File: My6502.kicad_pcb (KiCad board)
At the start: 2 copper layers, 99.7 x 99.7 mm, 28 parts, among them J1 IRQ_SEL, J2 CLK Jumper, J4 Expansion Port, J5 IRQ_Pullup, SW1 RESET, U1 ROM 28C256, U2 CPU 6502, U3 RAM 62256, U4 74HCT00, U5 74HCT02, U6 DS1813-10, U7 74LS21, X1 CXO_DIP14

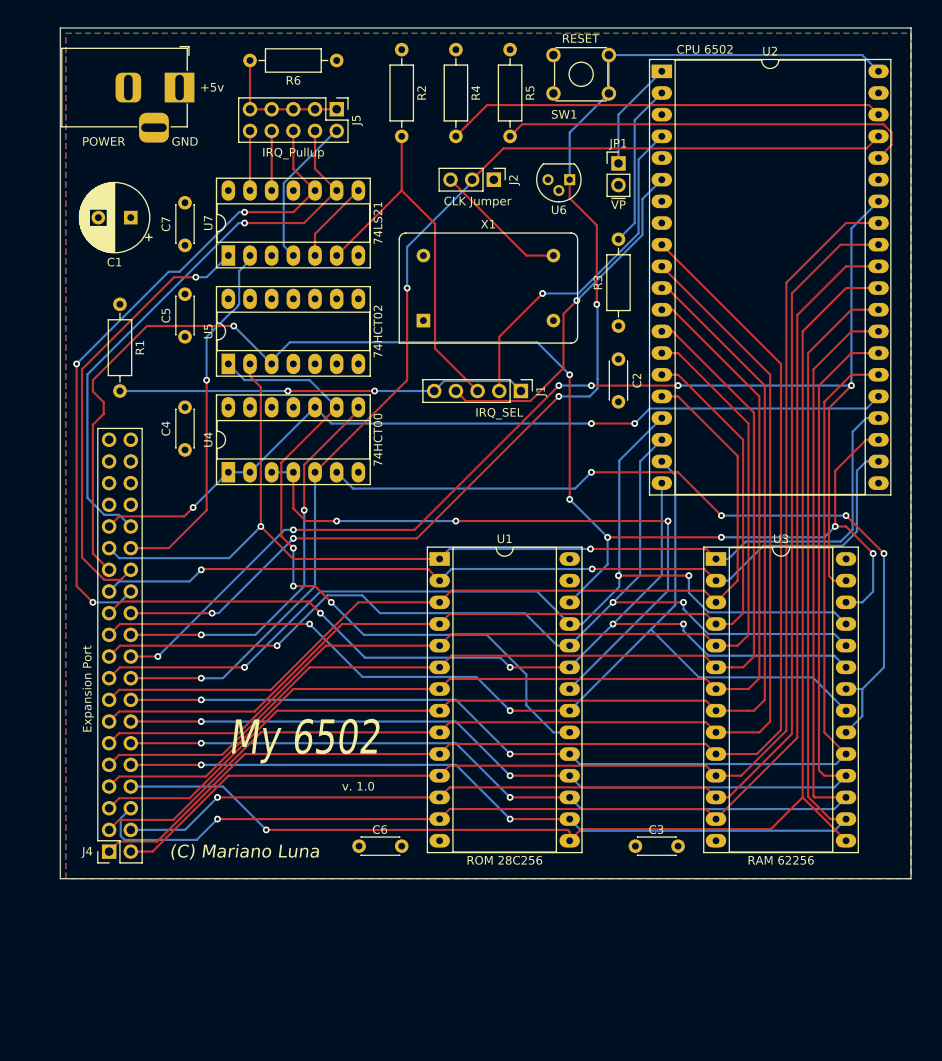
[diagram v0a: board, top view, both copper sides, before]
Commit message: Components Placed - missing wiring the VIA
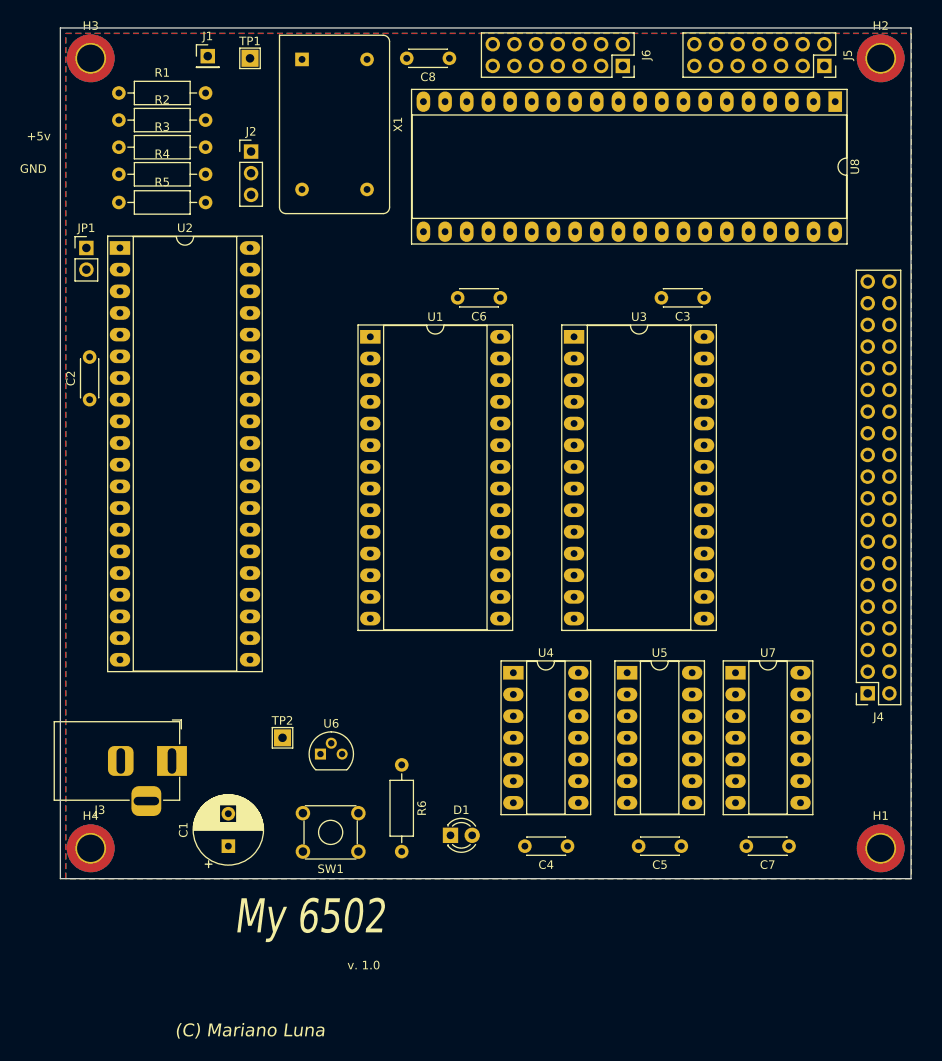
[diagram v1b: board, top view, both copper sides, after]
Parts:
- removed POWER: Barrel_Jack_Switch, Connector_BarrelJack:BarrelJack_Horizontal
- added C8: 0.1uF, Capacitor_THT:C_Disc_D4.3mm_W1.9mm_P5.00mm, F.Cu at (76.7, 53.7)
- added D1: LED, LED_THT:LED_D3.0mm, F.Cu at (76.8, 144.8)
- added H1: MNT, MountingHole:MountingHole_3.2mm_M3_DIN965_Pad_TopBottom, F.Cu at (127.3, 146.3)
- added H2: MNT, MountingHole:MountingHole_3.2mm_M3_DIN965_Pad_TopBottom, F.Cu at (127.3, 53.7)
- added H3: MNT, MountingHole:MountingHole_3.2mm_M3_DIN965_Pad_TopBottom, F.Cu at (34.7, 53.7)
- added H4: MNT, MountingHole:MountingHole_3.2mm_M3_DIN965_Pad_TopBottom, F.Cu at (34.7, 146.3)
- added J3: Power 5V, Connector_BarrelJack:BarrelJack_Horizontal, F.Cu at (44.2, 136.1)
- added J6: Port B, Connector_PinSocket_2.54mm:PinSocket_2x07_P2.54mm_Vertical, F.Cu at (97.0, 54.6)
- added TP1: CLK, TestPoint:TestPoint_THTPad_2.0x2.0mm_Drill1.0mm, F.Cu at (53.3, 53.7)
- added TP2: ~RESET, TestPoint:TestPoint_THTPad_2.0x2.0mm_Drill1.0mm, F.Cu at (57.1, 133.3)
- added U8: WD65C22, Package_DIP:DIP-40_W15.24mm_Socket_LongPads, F.Cu at (121.9, 58.8)
- C1: value 1000uF -> 100uF
- J1: value IRQ_SEL -> ~NMI; footprint Connector_PinHeader_2.54mm:PinHeader_1x05_P2.54mm_Vertical -> Connector_PinHeader_2.54mm:PinHeader_1x01_P2.54mm_Vertical
- J4: value Expansion Port -> Expansion Bus
- J5: value IRQ_Pullup -> Port A; footprint Connector_PinHeader_2.54mm:PinHeader_2x05_P2.54mm_Vertical -> Connector_PinSocket_2.54mm:PinSocket_2x07_P2.54mm_Vertical
- R1, R2, R3, R4, R5: value 4K7 -> 3K3
- R6: value 4K7 -> 150
- U2: value CPU 6502 -> WD65C02; footprint Package_DIP:DIP-40_W25.4mm_Socket_LongPads -> Package_DIP:DIP-40_W15.24mm_Socket_LongPads
- X1: value CXO_DIP14 -> OSC
- moved C7 99.8 mm to (116.5, 146.1), turned to 180 degrees
- moved SW1 96.1 mm to (66.0, 146.7), turned to 180 degrees
- moved J4 90.8 mm to (125.7, 128.1)
- moved C5 83.3 mm to (103.9, 146.1), turned to 180 degrees
- moved R6 82.9 mm to (71.1, 136.5), turned to 270 degrees
- moved U7 77.0 mm to (110.2, 125.7), turned to 0 degrees
- moved C1 74.5 mm to (50.8, 146.1), turned to 90 degrees
- moved U6 73.4 mm to (61.6, 135.3), turned to 0 degrees
- moved U2 66.8 mm to (38.1, 75.9)
- moved C6 66.4 mm to (82.7, 81.8), turned to 180 degrees
- moved C3 64.8 mm to (106.6, 81.8), turned to 180 degrees
- moved C4 64.5 mm to (90.6, 146.1), turned to 180 degrees
- moved JP1 63.1 mm to (34.2, 75.9)
- moved R3 62.2 mm to (38.0, 64.1), turned to 0 degrees
- moved C2 62.2 mm to (34.5, 93.7), turned to 90 degrees
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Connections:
- net /CLK_OUT renamed Net-(J2-Pad3)
- J1 pad 1: Net-(J1-Pad1) -> ~NMI
- J4 pad 1: a0 -> GND
- J4 pad 10: d4 -> d3
- J4 pad 11: a5 -> a4
- J4 pad 12: d5 -> d4
- J4 pad 13: a6 -> a5
- J4 pad 14: d6 -> d5
- J4 pad 15: a7 -> a6
- J4 pad 16: d7 -> d6
- J4 pad 17: a8 -> a7
- J4 pad 18: CLK -> d7
- J4 pad 19: a9 -> a8
- J4 pad 2: d0 -> +5V
- J4 pad 20: R~W -> PHI2
- J4 pad 21: a10 -> a9
- J4 pad 22: ~IO_CS -> R~W
- J4 pad 23: a11 -> a10
- J4 pad 24: ~RESET -> ~IO_CS
- J4 pad 25: a12 -> a11
- J4 pad 26: EXP_IRQ -> ~RESET
- J4 pad 27: a13 -> a12
- J4 pad 28: ~VIA1_IRQ -> ~VIA2_IRQ
- J4 pad 29: a14 -> a13
- J4 pad 3: a1 -> a0
- J4 pad 30: ~VIA2_IRQ -> EXP_IRQ
- J4 pad 31: a15 -> a14
- J4 pad 33: Net-(J4-Pad33) -> a15
- J4 pad 34: Net-(J4-Pad34) -> ~NMI
- J4 pad 38: GND -> Net-(J4-Pad38)
- J4 pad 39: Net-(J4-Pad39) -> +5V
- J4 pad 4: d1 -> d0
- J4 pad 40: +5V -> GND
- J4 pad 5: a2 -> a1
- J4 pad 6: d2 -> d1
- J4 pad 7: a3 -> a2
- J4 pad 8: d3 -> d2
- J4 pad 9: a4 -> a3
- J5 pad 1: Net-(J5-Pad1) -> GND
- J5 pad 10: Net-(J5-Pad10) -> PA7
- J5 pad 2: Net-(J5-Pad2) -> +5V
- J5 pad 3: Net-(J5-Pad1) -> PA0
- J5 pad 4: ~ACIA_IRQ -> PA1
- J5 pad 5: Net-(J5-Pad1) -> PA2
- J5 pad 6: EXP_IRQ -> PA3
- J5 pad 7: Net-(J5-Pad1) -> PA4
- J5 pad 8: Net-(J5-Pad8) -> PA5
- J5 pad 9: Net-(J5-Pad1) -> PA6
- JP1 pad 2: +5V -> GND
- R1 pad 2: Net-(J1-Pad1) -> ~NMI
- R6 pad 2: Net-(J5-Pad1) -> Net-(D1-Pad2)
- U2 pad 39: Net-(U2-Pad39) -> PHI2
- U2 pad 4: Net-(J1-Pad2) -> ~IRQ
- U2 pad 6: Net-(J1-Pad4) -> ~NMI
- U4 pad 5: CLK -> PHI2
- U7 pad 10: EXP_IRQ -> GND
- U7 pad 12: Net-(J5-Pad8) -> GND
- U7 pad 13: Net-(J5-Pad10) -> GND
- U7 pad 4: Net-(J5-Pad2) -> ~ACIA_IRQ
- U7 pad 5: Net-(U7-Pad5) -> EXP_IRQ
- U7 pad 8: Net-(U7-Pad5) -> Net-(U7-Pad8)
- U7 pad 9: ~ACIA_IRQ -> GND
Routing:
- net a13: track 171.9 -> 0.00 mm, vias 7 -> 0
- net d3: track 156.9 -> 0.00 mm, vias 1 -> 0
- net d4: track 155.5 -> 0.00 mm, vias 2 -> 0
- net d5: track 150.9 -> 0.00 mm, vias 2 -> 0
- net d2: track 150.6 -> 0.00 mm, vias 1 -> 0
- net d0: track 149.9 -> 0.00 mm
- net a0: track 148.3 -> 0.00 mm
- net d1: track 147.2 -> 0.00 mm, vias 1 -> 0
- net R~W: track 146.1 -> 0.00 mm, vias 6 -> 0
- net d6: track 144.7 -> 0.00 mm, vias 2 -> 0
- net a1: track 142.3 -> 0.00 mm
- net ~RESET: track 140.3 -> 0.00 mm, vias 4 -> 0
- net d7: track 137.4 -> 0.00 mm, vias 2 -> 0
- net a2: track 136.7 -> 0.00 mm
- net a3: track 131.1 -> 0.00 mm
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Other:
- rule trace_min: 0.2 -> 0.1524

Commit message: PCB done minus VIA Registers - DRC Passing
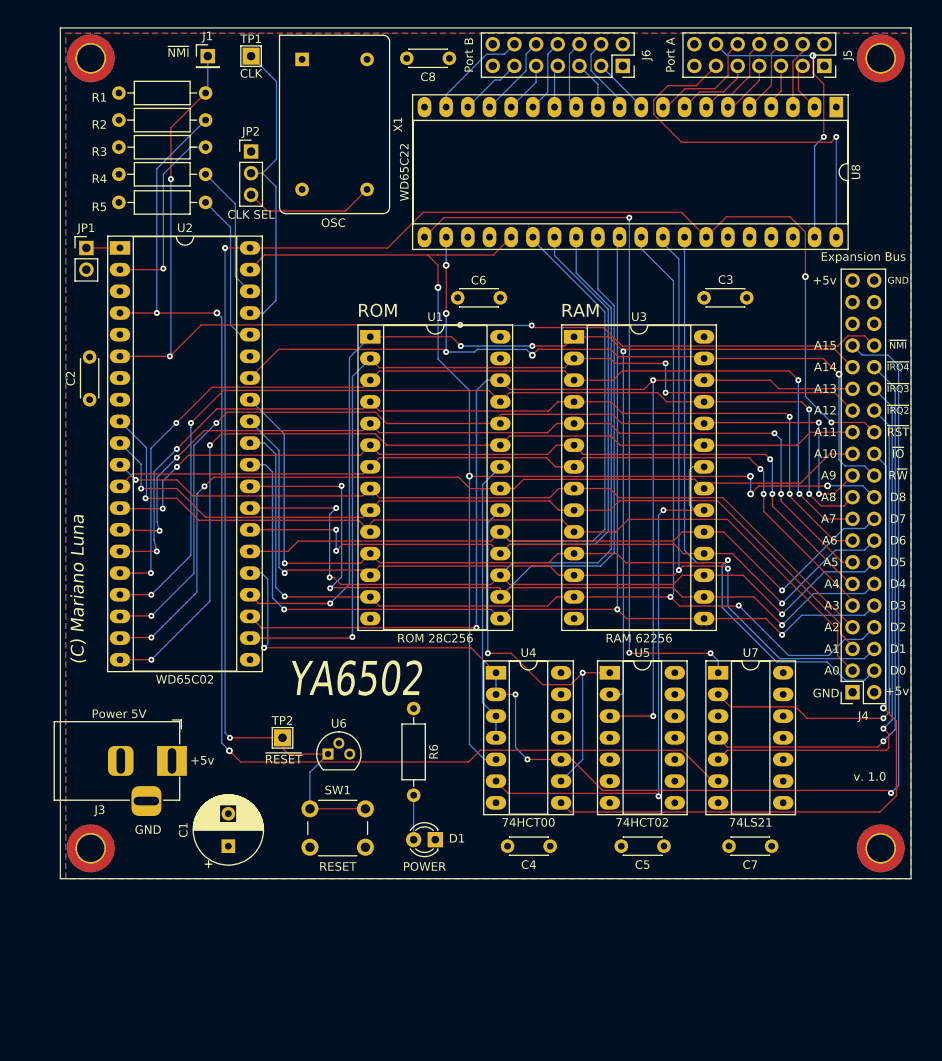
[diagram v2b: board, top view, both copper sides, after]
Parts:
- D1: value LED -> POWER
- JP2: renamed from J2; value CLK Jumper -> CLK SEL
- SW1: footprint Button_Switch_THT:SW_TH_Tactile_Omron_B3F-10xx -> Button_Switch_THT:SW_PUSH_6mm_H5mm
- moved R6 6.75 mm to (72.5, 129.9)
- moved U7 2.03 mm to (108.2, 125.7)
- moved C4 2.03 mm to (88.5, 146.1)
- moved C5 2.03 mm to (101.9, 146.1)
- moved C7 2.03 mm to (114.5, 146.1)
- moved U4 2.03 mm to (82.2, 125.7)
- moved U5 2.03 mm to (95.5, 125.7)
- moved D1 1.85 mm to (75.1, 145.3), turned to 180 degrees
- moved J4 1.78 mm to (124.0, 128.0)
- moved SW1 0.97 mm to (66.9, 146.2)
- moved U6 0.89 mm to (62.5, 135.3)
- moved U8 0.65 mm to (122.0, 59.4)
- moved TP1 0.28 mm to (53.5, 53.5)
- turned C3 to 0 degrees
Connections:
- net Net-(J2-Pad3) renamed /OSC_OUT
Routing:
- net ~RESET: track 0.00 -> 186.2 mm, vias 0 -> 4
- net a15: track 0.00 -> 153.1 mm, vias 0 -> 4
- net ~IRQ: track 0.00 -> 148.1 mm, vias 0 -> 3
- net PHI2: track 0.00 -> 145.8 mm, vias 0 -> 5
- net d4: track 0.00 -> 145.6 mm, vias 0 -> 3
- net a13: track 0.00 -> 145.3 mm, vias 0 -> 3
- net d0: track 0.00 -> 144.9 mm, vias 0 -> 2
- net a14: track 0.00 -> 143.7 mm, vias 0 -> 4
- net d5: track 0.00 -> 141.0 mm, vias 0 -> 3
- net d2: track 0.00 -> 138.8 mm, vias 0 -> 3
- net d1: track 0.00 -> 137.7 mm, vias 0 -> 3
- net d3: track 0.00 -> 136.1 mm, vias 0 -> 3
- net d6: track 0.00 -> 133.6 mm, vias 0 -> 3
- net d7: track 0.00 -> 132.3 mm, vias 0 -> 1
- net ~NMI: track 0.00 -> 129.0 mm, vias 0 -> 4
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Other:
- board text added: "A0"
- board text added: "A1"
- board text added: "A10"
- board text added: "A11"
- board text added: "A12"
- board text added: "A13"
- board text added: "A14"
- board text added: "A15"
- board text added: "A2"
- board text added: "A3"
- board text added: "A4"
- board text added: "A5"
- board text added: "A6"
- board text added: "A7"
- board text added: "A8"
- board text added: "A9"
- board text added: "D0"
- board text added: "D1"
- board text added: "D2"
- board text added: "D3"
- board text added: "D4"
- board text added: "D5"
- board text added: "D6"
- board text added: "D7"
- board text added: "D8"
- board text added: "RAM"
- board text added: "ROM"
- board text added: "R~W"
- board text added: "YA6502"
- board text added: "~IO"
- board text added: "~IRQ2"
- board text added: "~IRQ3"
- board text added: "~IRQ4"
- board text added: "~NMI"
- board text added: "~RST"
- board text removed: "My 6502"

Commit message: V1.5 Ready - Full board CPU,RAM,ROM,VIA
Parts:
- U1: renamed from U2; value WD65C02 -> 6502
- renumbered C2 to C1, C6 to C2, C7 to C6, C8 to C7, C1 to C8, U1 to U2, U7 to U6, U8 to U7, U6 to U8
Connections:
- U7 pad 23: Net-(U8-Pad23) -> ~IO_CS
- U7 pad 24: Net-(U8-Pad24) -> a12
- U7 pad 35: Net-(U8-Pad35) -> a3
- U7 pad 36: Net-(U8-Pad36) -> a2
- U7 pad 37: Net-(U8-Pad37) -> a1
- U7 pad 38: Net-(U8-Pad38) -> a0
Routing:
- net ~IO_CS: track 81.9 -> 154.5 mm, vias 1 -> 4
- net a0: track 106.3 -> 147.6 mm, vias 1 -> 3
- net a1: track 100.9 -> 140.9 mm, vias 1 -> 3
- net a2: track 95.3 -> 133.1 mm, vias 1 -> 3
- net a3: track 98.4 -> 127.9 mm, vias 2 -> 3
- net a12: track 107.6 -> 135.3 mm, vias 3 -> 4
- net ~VIA1_IRQ: track 88.1 -> 89.8 mm
- net ~RESET: track 186.2 -> 187.8 mm
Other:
- board text added: "+ JP1: Closed NMOS | Open CMOS + JP2: 1. GND | 2. PHI2 IN | 3. OSC OUT 1Mhz + J1: ~NMI IN"
- board text added: "- RAM $0000-$7FFF 32K - I/O $8000-$9FFF 8K - VIA1 $9000 - $900F - ROM $A000-$FFFF 24K"
- board text added: "CPU 6502"
- board text added: "VIA1 $9000 - $900F"
- board text added: "YAsixfive02"
- board text added: "v. 1.5"
- board text removed: "YA6502"
- board text removed: "v. 1.0"
